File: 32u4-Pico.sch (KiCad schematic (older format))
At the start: 27 parts, among them J3 2.54mm header 01x20, J4 2.54mm header 01x20, U1 ATmega32U4-MU, U2 3.3VO SOT-23, X1 8Mhz 3225

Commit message: implemented Rest pin in place of RUN and added a reset button + a couple other bits
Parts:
- removed R10: 1Ohm 0402, Resistor_SMD:R_0402_1005Metric, symbol Device:R_Small
- removed R9: 200ohm 0603, Resistor_SMD:R_0603_1608Metric, symbol Device:R_Small
- added R1: 10K 0402, Resistor_SMD:R_0402_1005Metric, symbol Device:R_Small
- added RSW1: SKRK, Button_Switch_SMD:SW_Push_SPST_NO_Alps_SKRK, symbol Switch:SW_Push
- R3, R4: value 27Ohms 0402 Resistor -> 22Ohm 0402 Resistor
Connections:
- net labels removed: XOUT
- wire segments 125 -> 128
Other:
- note removed: "Intentionally left floating"
- note removed: "Make sure C10 is close to pin 44 of RP2040"
- note removed: "Pin1 on XO Oscillator also left floating so the chip is enabled\n(this is specified in their datasheet)"
- note removed: "Use a 12mhz Seiko Oscilator, 3225-4Pin"
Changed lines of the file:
@@
 encoding utf-8
 Sheet 1 1
-Title "RP2040 Minimal Design Example"
+Title ""
 Date "2020-12-18"
-Rev "REV1"
-Comp "Raspberry Pi (Trading) Ltd"
+Rev ""
+Comp ""
 Comment1 ""
 Comment2 ""
@@
 Text Label 3850 8400 2    50   ~ 0
 XIN
-Text Label 3900 9000 2    50   ~ 0
-XOUT
 Wire Wire Line
 	2600 8400 3200 8400
@@
 	-1   0    0    1
 $EndComp
-Wire Wire Line
-	3650 9000 3900 9000
-Text Notes 3450 8900 0    39   ~ 0
-Intentionally left floating
-Text Notes 1700 9250 0    50   ~ 0
-Pin1 on XO Oscillator also left floating so the chip is enabled\n(this is specified in their datasheet)
 Text GLabel 1100 2400 2    50   Input ~ 0
 GND
@@
 	1    0    0    -1
 $EndComp
-Text Notes 1700 9350 0    50   ~ 0
-Use a 12mhz Seiko Oscilator, 3225-4Pin
 Text Notes 3200 8650 0    50   ~ 0
 Dont bother trying to use a crystal\nas it massively complicates this clock source setup
@@
 Wire Wire Line
 	6900 5350 6450 5350
-Text Label 9550 2050 0    50   ~ 0
-ADC_VREF
-Wire Wire Line
-	9250 2050 9250 2150
-Wire Wire Line
-	9250 2050 9550 2050
-Connection ~ 9250 2050
-Wire Wire Line
-	9250 1900 9250 2050
-Wire Wire Line
-	9250 1600 9250 1700
-$Comp
-L Device:R_Small R9
-U 1 1 61044B24
-P 9250 1800
-F 0 "R9" H 9309 1846 50  0000 L CNN
-F 1 "200ohm 0603" H 9309 1755 50  0000 L CNN
-F 2 "Resistor_SMD:R_0603_1608Metric" H 9250 1800 50  0001 C CNN
-F 3 "~" H 9250 1800 50  0001 C CNN
-	1    9250 1800
-	1    0    0    -1
-$EndComp
-$Comp
-L Device:R_Small R10
-U 1 1 610441D8
-P 9250 2250
-F 0 "R10" H 9309 2296 50  0000 L CNN
-F 1 "1Ohm 0402" H 9309 2205 50  0000 L CNN
-F 2 "Resistor_SMD:R_0402_1005Metric" H 9250 2250 50  0001 C CNN
-F 3 "~" H 9250 2250 50  0001 C CNN
-	1    9250 2250
-	1    0    0    -1
-$EndComp
 Wire Wire Line
 	8850 2550 8850 2500
@@
 Connection ~ 7600 2500
 Wire Wire Line
-	7600 2450 7600 2500
-Wire Wire Line
 	7600 2500 7600 3100
 Wire Wire Line
@@
 P 6300 5350
 F 0 "R4" V 6300 5400 50  0000 C CNN
-F 1 " 27Ohms 0402 Resistor" V 6200 5350 50  0000 C CNN
+F 1 "22Ohm 0402 Resistor" V 6200 5350 50  0000 C CNN
 F 2 "Capacitor_SMD:C_0402_1005Metric" V 6230 5350 50  0001 C CNN
 F 3 "" H 6300 5350 50  0001 C CNN
@@
 P 6400 5250
 F 0 "R3" V 6400 5300 50  0000 C CNN
-F 1 " 27Ohms  0402 Resistor" V 6500 5300 50  0000 C CNN
+F 1 " 22Ohm  0402 Resistor" V 6500 5300 50  0000 C CNN
 F 2 "Capacitor_SMD:C_0402_1005Metric" V 6330 5250 50  0001 C CNN
 F 3 "" H 6400 5250 50  0001 C CNN
@@
 	0    -1   -1   0
 $EndComp
-Text GLabel 7600 2450 0    39   Input ~ 0
-VSYS
-Text GLabel 9250 1600 0    39   Input ~ 0
+Text GLabel 7500 2350 0    39   Input ~ 0
 VSYS
 Text Label 6750 4450 2    50   ~ 0
@@
 	1    0    0    -1
 $EndComp
-Text Notes 8100 3150 0    50   ~ 0
-Make sure C10 is close to pin 44 of RP2040
-Wire Wire Line
-	9250 2350 9250 2500
 Connection ~ 9250 2500
 Wire Wire Line
@@
 U 1 1 6122812D
 P 6250 4850
-F 0 "C3" H 6365 4896 50  0000 L CNN
-F 1 "1uf 0402" H 6365 4805 50  0000 L CNN
+F 0 "C3" V 6300 4700 50  0000 L CNN
+F 1 "1uf 0402" V 6100 4550 50  0000 L CNN
 F 2 "Capacitor_SMD:C_0402_1005Metric" H 6288 4700 50  0001 C CNN
 F 3 "" H 6250 4850 50  0001 C CNN
@@
 Text Label 8600 7050 2    50   ~ 0
 GPIO21
+$Comp
+L Device:R_Small R1
+U 1 1 610E95DF
+P 6700 3850
+F 0 "R1" H 6759 3896 50  0000 L CNN
+F 1 "10K 0402" H 6759 3805 50  0000 L CNN
+F 2 "Resistor_SMD:R_0402_1005Metric" H 6700 3850 50  0001 C CNN
+F 3 "~" H 6700 3850 50  0001 C CNN
+	1    6700 3850
+	1    0    0    -1
+$EndComp
+Text GLabel 6650 3700 0    39   Input ~ 0
+VSYS
+Wire Wire Line
+	6900 4250 6700 4250
+$Comp
+L Switch:SW_Push RSW1
+U 1 1 610FBDD2
+P 6200 4250
+F 0 "RSW1" H 6200 4535 50  0000 C CNN
+F 1 "SKRK" H 6200 4444 50  0000 C CNN
+F 2 "Button_Switch_SMD:SW_Push_SPST_NO_Alps_SKRK" H 6200 4450 50  0001 C CNN
+F 3 "~" H 6200 4450 50  0001 C CNN
+	1    6200 4250
+	1    0    0    -1
+$EndComp
+$Comp
+L power:GND #PWR01
+U 1 1 610FC4BB
+P 5950 4250
+F 0 "#PWR01" H 5950 4000 50  0001 C CNN
+F 1 "GND" V 5955 4122 50  0000 R CNN
+F 2 "" H 5950 4250 50  0001 C CNN
+F 3 "" H 5950 4250 50  0001 C CNN
+	1    5950 4250
+	0    1    1    0
+$EndComp
+Wire Wire Line
+	5950 4250 6000 4250
+Wire Wire Line
+	6700 3950 6700 4250
+Connection ~ 6700 4250
+Wire Wire Line
+	6700 4250 6500 4250
+Wire Wire Line
+	6650 3700 6700 3700
+Wire Wire Line
+	6700 3700 6700 3750
+Text Label 6500 4200 2    50   ~ 0
+RUN
+Wire Wire Line
+	6500 4250 6500 4200
+Connection ~ 6500 4250
+Wire Wire Line
+	6500 4250 6400 4250
+Wire Wire Line
+	7500 2350 7600 2350
+Wire Wire Line
+	7600 2350 7600 2500
 $EndSCHEMATC

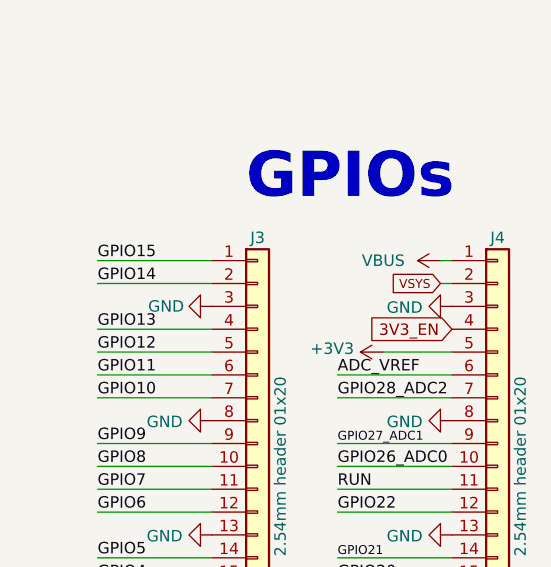
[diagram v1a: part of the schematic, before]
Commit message: Added keepout zones near the pin holes and corrected all errors as per DRC.
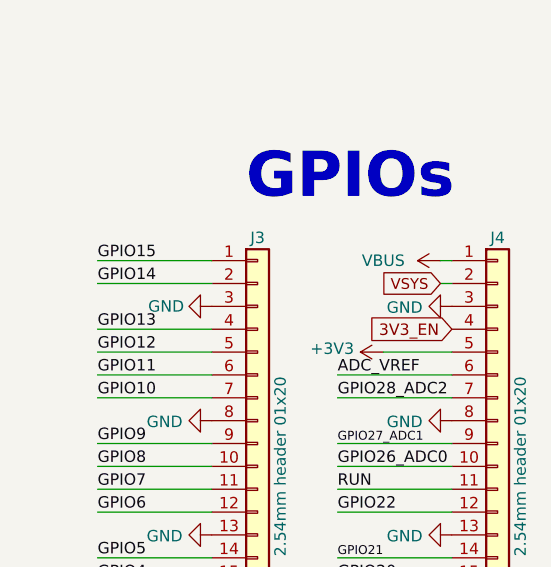
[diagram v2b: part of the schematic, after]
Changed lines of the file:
@@
 Wire Wire Line
 	2850 1750 3150 1750
-Text GLabel 14550 4800 0    39   Input ~ 0
+Text GLabel 14550 4800 0    47   Input ~ 0
 VSYS
 Wire Wire Line

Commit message: swapped oscillator for crystal because easier to get a hold of as of right now. (and a bit of tidying up)
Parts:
- removed C2: 15pf 0402, Capacitor_SMD:C_0402_1005Metric, symbol Device:C
- removed U2: 3.3VO SOT-23, Package_TO_SOT_SMD:SOT-23, symbol Regulator_Linear:LF33_TO220
- removed X1: 8Mhz 3225, Crystal:Crystal_SMD_SeikoEpson_TSX3225-4Pin_3.2x2.5mm, symbol Oscillator:XO32
- added C2, C7: 22pF 0402, Capacitor_SMD:C_0402_1005Metric, symbol Device:C_Small
- added Y1: 8MHz 3225_4p crystal, Crystal:Crystal_SMD_3225-4Pin_3.2x2.5mm, symbol Device:Crystal_GND24
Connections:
- net labels added: XTAL1, XTAL2
- net labels removed: +3.3V, XIN
- wire segments 128 -> 141
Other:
- note removed: "Dont bother trying to use a crystal\nas it massively complicates this clock source setup"
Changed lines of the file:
@@
 Text Notes 13700 4450 0    197  ~ 39
 GPIOs
-Text Label 3850 8400 2    50   ~ 0
-XIN
-Wire Wire Line
-	2600 8400 3200 8400
 Wire Wire Line
 	13550 6600 13050 6600
@@
 	0    1    1    0
 $EndComp
-$Comp
-L Oscillator:XO32 X1
-U 1 1 60894744
-P 2600 8700
-F 0 "X1" V 2250 8550 50  0000 L CNN
-F 1 "8Mhz 3225" V 2350 8450 50  0000 L CNN
-F 2 "Crystal:Crystal_SMD_SeikoEpson_TSX3225-4Pin_3.2x2.5mm" H 3300 8350 50  0001 C CNN
-F 3 "" H 2500 8700 50  0001 C CNN
-	1    2600 8700
-	0    -1   -1   0
-$EndComp
-$Comp
-L power:GND #PWR0105
-U 1 1 608B9527
-P 2900 8700
-F 0 "#PWR0105" H 2900 8450 50  0001 C CNN
-F 1 "GND" V 2905 8572 50  0000 R CNN
-F 2 "" H 2900 8700 50  0001 C CNN
-F 3 "" H 2900 8700 50  0001 C CNN
-	1    2900 8700
-	0    -1   -1   0
-$EndComp
-$Comp
-L power:+3.3V #PWR0106
-U 1 1 608B9D1F
-P 2300 8700
-F 0 "#PWR0106" H 2300 8550 50  0001 C CNN
-F 1 "+3.3V" V 2315 8828 50  0000 L CNN
-F 2 "" H 2300 8700 50  0001 C CNN
-F 3 "" H 2300 8700 50  0001 C CNN
-	1    2300 8700
-	0    -1   -1   0
-$EndComp
-$Comp
-L Device:C C2
-U 1 1 5ED96B87
-P 3200 8250
-F 0 "C2" H 3315 8296 50  0000 L CNN
-F 1 "15pf 0402" H 3315 8205 50  0000 L CNN
-F 2 "Capacitor_SMD:C_0402_1005Metric" H 3238 8100 50  0001 C CNN
-F 3 "" H 3200 8250 50  0001 C CNN
-	1    3200 8250
-	1    0    0    -1
-$EndComp
-Connection ~ 3200 8400
-Wire Wire Line
-	3200 8400 3850 8400
-$Comp
-L power:GND #PWR0107
-U 1 1 6097CBA8
-P 3200 8100
-F 0 "#PWR0107" H 3200 7850 50  0001 C CNN
-F 1 "GND" H 3205 7927 50  0000 C CNN
-F 2 "" H 3200 8100 50  0001 C CNN
-F 3 "" H 3200 8100 50  0001 C CNN
-	1    3200 8100
-	-1   0    0    1
-$EndComp
 Text GLabel 1100 2400 2    50   Input ~ 0
 GND
@@
 	1    0    0    -1
 $EndComp
-Text Notes 3200 8650 0    50   ~ 0
-Dont bother trying to use a crystal\nas it massively complicates this clock source setup
 Text Notes 600  750  0    50   ~ 0
 2x 5.1K Resistors on the CC pins will = 5V@1.5A\nthis is the recomended default config for type-c
@@
 Text GLabel 7500 2350 0    39   Input ~ 0
 VSYS
-Text Label 6750 4450 2    50   ~ 0
-XIN
-Wire Wire Line
-	6750 4450 6900 4450
 Text GLabel 6900 5050 0    39   Input ~ 0
 VBUS
@@
 Text Label 8600 5950 2    50   ~ 0
 GPIO10
-$Comp
-L Regulator_Linear:LF33_TO220 U2
-U 1 1 61280791
-P 1100 8700
-F 0 "U2" H 1100 8942 50  0000 C CNN
-F 1 "3.3VO SOT-23" H 1100 8851 50  0000 C CNN
-F 2 "Package_TO_SOT_SMD:SOT-23" H 1100 8925 50  0001 C CIN
-F 3 "http://www.st.com/content/ccc/resource/technical/document/datasheet/c4/0e/7e/2a/be/bc/4c/bd/CD00000546.pdf/files/CD00000546.pdf/jcr:content/translations/en.CD00000546.pdf" H 1100 8650 50  0001 C CNN
-	1    1100 8700
-	1    0    0    -1
-$EndComp
-$Comp
-L power:+3.3V #PWR0111
-U 1 1 612816FB
-P 1400 8700
-F 0 "#PWR0111" H 1400 8550 50  0001 C CNN
-F 1 "+3.3V" V 1415 8828 50  0000 L CNN
-F 2 "" H 1400 8700 50  0001 C CNN
-F 3 "" H 1400 8700 50  0001 C CNN
-	1    1400 8700
-	0    1    1    0
-$EndComp
-$Comp
-L power:GND #PWR0112
-U 1 1 6128B908
-P 1100 9000
-F 0 "#PWR0112" H 1100 8750 50  0001 C CNN
-F 1 "GND" H 1100 8800 50  0000 C CNN
-F 2 "" H 1100 9000 50  0001 C CNN
-F 3 "" H 1100 9000 50  0001 C CNN
-	1    1100 9000
-	1    0    0    -1
-$EndComp
 Wire Wire Line
 	8100 5650 8600 5650
@@
 $EndComp
 Connection ~ 9900 2950
-Text GLabel 800  8700 0    50   Input ~ 0
-VSYS
 Wire Wire Line
 	8100 4850 8600 4850
@@
 Wire Wire Line
 	7600 2350 7600 2500
+Text GLabel 6900 4450 0    50   Input ~ 0
+XTAL1
+Text GLabel 6900 4650 0    50   Input ~ 0
+XTAL2
+Text GLabel 1600 8800 0    50   Input ~ 0
+XTAL1
+Text GLabel 1600 9000 0    50   Input ~ 0
+XTAL2
+$Comp
+L Device:Crystal_GND24 Y1
+U 1 1 611E12C9
+P 1900 8900
+F 0 "Y1" V 1900 8850 50  0000 L CNN
+F 1 "8MHz 3225_4p crystal" V 1950 9100 20  0000 L CNN
+F 2 "Crystal:Crystal_SMD_3225-4Pin_3.2x2.5mm" H 1900 8900 50  0001 C CNN
+F 3 "~" H 1900 8900 50  0001 C CNN
+	1    1900 8900
+	0    1    1    0
+$EndComp
+Wire Wire Line
+	1600 9000 1650 9000
+Wire Wire Line
+	1650 9000 1650 9100
+Wire Wire Line
+	1650 9100 1900 9100
+Wire Wire Line
+	1600 8800 1650 8800
+Wire Wire Line
+	1650 8800 1650 8700
+Wire Wire Line
+	1650 8700 1900 8700
+Wire Wire Line
+	1900 8750 1900 8700
+Wire Wire Line
+	1900 9050 1900 9100
+$Comp
+L power:GND #PWR02
+U 1 1 611FE0D7
+P 1700 8900
+F 0 "#PWR02" H 1700 8650 50  0001 C CNN
+F 1 "GND" V 1705 8772 50  0000 R CNN
+F 2 "" H 1700 8900 50  0001 C CNN
+F 3 "" H 1700 8900 50  0001 C CNN
+	1    1700 8900
+	0    1    1    0
+$EndComp
+$Comp
+L Device:C_Small C2
+U 1 1 611FFE4A
+P 2200 8700
+F 0 "C2" V 1971 8700 50  0000 C CNN
+F 1 "22pF 0402" V 2062 8700 50  0000 C CNN
+F 2 "Capacitor_SMD:C_0402_1005Metric" H 2200 8700 50  0001 C CNN
+F 3 "~" H 2200 8700 50  0001 C CNN
+	1    2200 8700
+	0    1    1    0
+$EndComp
+$Comp
+L Device:C_Small C7
+U 1 1 612008C3
+P 2200 9100
+F 0 "C7" V 2300 9100 50  0000 C CNN
+F 1 "22pF 0402" V 2400 9100 50  0000 C CNN
+F 2 "Capacitor_SMD:C_0402_1005Metric" H 2200 9100 50  0001 C CNN
+F 3 "~" H 2200 9100 50  0001 C CNN
+	1    2200 9100
+	0    1    1    0
+$EndComp
+Wire Wire Line
+	1900 8700 2100 8700
+Connection ~ 1900 8700
+Wire Wire Line
+	1900 9100 2100 9100
+Connection ~ 1900 9100
+Wire Wire Line
+	2300 9100 2450 9100
+Wire Wire Line
+	2450 9100 2450 8900
+Wire Wire Line
+	2450 8700 2300 8700
+Wire Wire Line
+	2100 8900 2450 8900
+Connection ~ 2450 8900
+Wire Wire Line
+	2450 8900 2450 8700
+$Comp
+L power:GND #PWR05
+U 1 1 61224AC9
+P 2550 8900
+F 0 "#PWR05" H 2550 8650 50  0001 C CNN
+F 1 "GND" V 2555 8772 50  0000 R CNN
+F 2 "" H 2550 8900 50  0001 C CNN
+F 3 "" H 2550 8900 50  0001 C CNN
+	1    2550 8900
+	0    -1   -1   0
+$EndComp
+Wire Wire Line
+	2450 8900 2550 8900
 $EndSCHEMATC

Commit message: small adjustment fix for the vbus/vsys diode.
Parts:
- D1: value Schottky 0603 -> 1n40002; footprint Diode_SMD:D_0603_1608Metric -> Diode_SMD:D_SOD-123
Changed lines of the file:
@@
 P 2450 1750
 F 0 "D1" H 2450 1533 50  0000 C CNN
-F 1 "Schottky 0603" H 2450 1624 50  0000 C CNN
-F 2 "Diode_SMD:D_0603_1608Metric" H 2450 1750 50  0001 C CNN
+F 1 "1n40002" H 2450 1624 50  0000 C CNN
+F 2 "Diode_SMD:D_SOD-123" H 2450 1750 50  0001 C CNN
 F 3 "~" H 2450 1750 50  0001 C CNN
 	1    2450 1750

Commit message: Added ISP header in schematic.
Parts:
- added ISP: Conn_02x03_Odd_Even, symbol Connector_Generic:Conn_02x03_Odd_Even
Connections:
- net GND: now also ISP.6 (Pin_6)
- net VSYS: now also ISP.2 (Pin_2)
- net GPIO2 renamed GPIO2-SCK
- net GPIO2-SCK: now also ISP.3 (Pin_3)
- net GPIO3 renamed GPIO3-mosi
- net GPIO3-mosi: now also ISP.4 (Pin_4)
- net GPIO4 renamed GPIO4-miso
- net GPIO4-miso: now also ISP.1 (Pin_1)
- net RUN renamed RUN-RESET
- net RUN-RESET: now also ISP.5 (Pin_5)
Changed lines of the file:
@@
 Wire Wire Line
 	6700 3700 6700 3750
-Text Label 6500 4200 2    50   ~ 0
+Text Label 6500 4350 2    50   ~ 0
 RUN
 Wire Wire Line
@@
 Wire Wire Line
 	2450 8900 2550 8900
+Text GLabel 8600 4550 2    50   Input ~ 0
+GPIO4-miso
+Text GLabel 8600 4450 2    50   Input ~ 0
+GPIO3-mosi
+Text GLabel 8600 4350 2    50   Input ~ 0
+GPIO2-SCK
+Text GLabel 6500 4200 1    39   Input ~ 0
+RUN-RESET
+$Comp
+L Connector_Generic:Conn_02x03_Odd_Even ISP
+U 1 1 613C4220
+P 14100 7400
+F 0 "ISP" H 14150 7717 50  0000 C CNN
+F 1 "Conn_02x03_Odd_Even" H 14150 7626 50  0000 C CNN
+F 2 "" H 14100 7400 50  0001 C CNN
+F 3 "~" H 14100 7400 50  0001 C CNN
+	1    14100 7400
+	1    0    0    -1
+$EndComp
+Text GLabel 13900 7400 0    50   Input ~ 0
+GPIO2-SCK
+Text GLabel 14400 7400 2    50   Input ~ 0
+GPIO3-mosi
+Text GLabel 13900 7300 0    50   Input ~ 0
+GPIO4-miso
+Text GLabel 13900 7500 0    47   Input ~ 0
+RUN-RESET
+$Comp
+L power:GND #PWR?
+U 1 1 613C70D0
+P 14400 7500
+F 0 "#PWR?" H 14400 7250 50  0001 C CNN
+F 1 "GND" V 14405 7372 50  0000 R CNN
+F 2 "" H 14400 7500 50  0001 C CNN
+F 3 "" H 14400 7500 50  0001 C CNN
+	1    14400 7500
+	0    -1   -1   0
+$EndComp
+Text GLabel 14400 7300 2    47   Input ~ 0
+VSYS
+Wire Wire Line
+	6500 4350 6500 4250
 $EndSCHEMATC

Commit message: added ISP header on board and routed traces for it.
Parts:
- removed ISP: Conn_02x03_Odd_Even, symbol Connector_Generic:Conn_02x03_Odd_Even
- added ISP1: AVR-ISP-6, Connector_PinHeader_2.54mm:PinHeader_2x03_P2.54mm_Vertical, symbol Connector:AVR-ISP-6
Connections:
- net GND: now also ISP1.6 (GND)
- net GPIO2-SCK: now also ISP1.3 (SCK)
- net GPIO3-mosi: now also ISP1.4 (MOSI)
- net GPIO4-miso: now also ISP1.1 (MISO)
- net RUN-RESET: now also ISP1.5 (~RST)
- net VSYS: now also ISP1.2 (VCC)
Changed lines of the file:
@@
 Text GLabel 6500 4200 1    39   Input ~ 0
 RUN-RESET
-$Comp
-L Connector_Generic:Conn_02x03_Odd_Even ISP
-U 1 1 613C4220
-P 14100 7400
-F 0 "ISP" H 14150 7717 50  0000 C CNN
-F 1 "Conn_02x03_Odd_Even" H 14150 7626 50  0000 C CNN
-F 2 "" H 14100 7400 50  0001 C CNN
-F 3 "~" H 14100 7400 50  0001 C CNN
-	1    14100 7400
-	1    0    0    -1
-$EndComp
-Text GLabel 13900 7400 0    50   Input ~ 0
+Text GLabel 13750 8100 3    50   Input ~ 0
 GPIO2-SCK
-Text GLabel 14400 7400 2    50   Input ~ 0
+Text GLabel 13850 8100 3    50   Input ~ 0
 GPIO3-mosi
-Text GLabel 13900 7300 0    50   Input ~ 0
+Text GLabel 13950 8100 3    50   Input ~ 0
 GPIO4-miso
-Text GLabel 13900 7500 0    47   Input ~ 0
+Text GLabel 13650 8100 3    47   Input ~ 0
 RUN-RESET
 $Comp
-L power:GND #PWR?
+L power:GND #PWR0105
 U 1 1 613C70D0
-P 14400 7500
-F 0 "#PWR?" H 14400 7250 50  0001 C CNN
-F 1 "GND" V 14405 7372 50  0000 R CNN
-F 2 "" H 14400 7500 50  0001 C CNN
-F 3 "" H 14400 7500 50  0001 C CNN
-	1    14400 7500
-	0    -1   -1   0
+P 13350 7600
+F 0 "#PWR0105" H 13350 7350 50  0001 C CNN
+F 1 "GND" V 13355 7472 50  0000 R CNN
+F 2 "" H 13350 7600 50  0001 C CNN
+F 3 "" H 13350 7600 50  0001 C CNN
+	1    13350 7600
+	0    1    1    0
 $EndComp
-Text GLabel 14400 7300 2    47   Input ~ 0
+Text GLabel 14250 7600 2    47   Input ~ 0
 VSYS
 Wire Wire Line
 	6500 4350 6500 4250
+$Comp
+L Connector:AVR-ISP-6 ISP1
+U 1 1 613C5EE0
+P 13750 7700
+F 0 "ISP1" V 13283 7750 50  0000 C CNN
+F 1 "AVR-ISP-6" V 13374 7750 50  0000 C CNN
+F 2 "Connector_PinHeader_2.54mm:PinHeader_2x03_P2.54mm_Vertical" V 13500 7750 50  0001 C CNN
+F 3 " ~" H 12475 7150 50  0001 C CNN
+	1    13750 7700
+	0    1    1    0
+$EndComp
 $EndSCHEMATC

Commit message: Generated updated gerber and stuff
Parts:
- renumbered e1 to USB1
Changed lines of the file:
@@
 $EndDescr
 $Comp
-L Type-C:HRO-TYPE-C-31-M-12 e1
+L Type-C:HRO-TYPE-C-31-M-12 USB1
 U 1 1 5EDB7D8D
 P 1000 1750
-F 0 "e1" H 750 2150 50  0000 R CNN
+F 0 "USB1" H 750 2150 50  0000 R CNN
 F 1 "TYPE-C-31-M-12" H 1250 950 50  0000 R CNN
 F 2 "HRO-TYPE-C31-M-12:HRO-TYPE-C-31-M-12" H 1150 1700 50  0001 C CNN

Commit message: added correct orientation USB TP Pads to match RPI PICO and my Pico clone
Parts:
- added TP1, TP2: TestPoint, TestPoint:TestPoint_Pad_2.0x2.0mm, symbol Connector:TestPoint
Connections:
- net USB_D+: now also TP1.1
- net USB_D-: now also TP2.1
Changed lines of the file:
@@
+	0    1    1    0
+$EndComp
+Text GLabel 1100 3400 0    47   Input ~ 0
+USB_D-
+Text GLabel 1100 3250 0    47   Input ~ 0
+USB_D+
+$Comp
+L Connector:TestPoint TP1
+U 1 1 61CFC7C5
+P 1100 3250
+F 0 "TP1" V 1054 3438 50  0000 L CNN
+F 1 "TestPoint" V 1145 3438 50  0000 L CNN
+F 2 "TestPoint:TestPoint_Pad_2.0x2.0mm" H 1300 3250 50  0001 C CNN
+F 3 "~" H 1300 3250 50  0001 C CNN
+	1    1100 3250
+	0    1    1    0
+$EndComp
+$Comp
+L Connector:TestPoint TP2
+U 1 1 61CFD722
+P 1100 3400
+F 0 "TP2" V 1054 3588 50  0000 L CNN
+F 1 "TestPoint" V 1145 3588 50  0000 L CNN
+F 2 "TestPoint:TestPoint_Pad_2.0x2.0mm" H 1300 3400 50  0001 C CNN
+F 3 "~" H 1300 3400 50  0001 C CNN
+	1    1100 3400
 	0    1    1    0
 $EndComp
